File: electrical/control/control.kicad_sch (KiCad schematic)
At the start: 43 parts, among them J1 USB4105-GF-A, J2 SWD, J3 TC2030-NL, J4 UART, J5 QWIIC, SW1 SYS, U1 USBLC6-2P6, U2 LP5912-3.3DRV, U3 W25Q16JVSNIQ, U4 RP2040, U5 ABPMRRV060MG2A3, Y1 ABM8-272-T3

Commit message: More PCB work
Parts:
- U3: value W25Q16JVSNIQ -> W25Q16JVUXIQ; footprint Package_SO:SOIC-8_3.9x4.9mm_P1.27mm -> Package_SON:Winbond_USON-8-1EP_3x2mm_P0.5mm_EP0.2x1.6mm; LCSC C115407 -> C2843335
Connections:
- net I2C_SCL: now also U4.14 (GPIO11); no longer U4.38 (GPIO26_ADC0)
- net I2C_SDA: now also U4.13 (GPIO10); no longer U4.39 (GPIO27_ADC1)
- net PRESSURE_INT: now also U4.12 (GPIO9); no longer U4.40 (GPIO28_ADC2)
- net UART_RX: now also R5.2; no longer R5.1
- net UART_TX: now also R4.2; no longer R4.1
- net at SW1.1: now also U4.36 (GPIO24); no longer U4.5 (GPIO3)
- net at U4.3 (GPIO1): no longer R5.2
- net at U4.2 (GPIO0): no longer R4.2
- net at U4.27 (GPIO16): now also R4.1
- net at U4.28 (GPIO17): now also R5.1
- net at U4.37 (GPIO25): now also R8.1
- net at U4.4 (GPIO2): no longer R8.1
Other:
- moved on the sheet: D1, R4, R5, R8, SW1

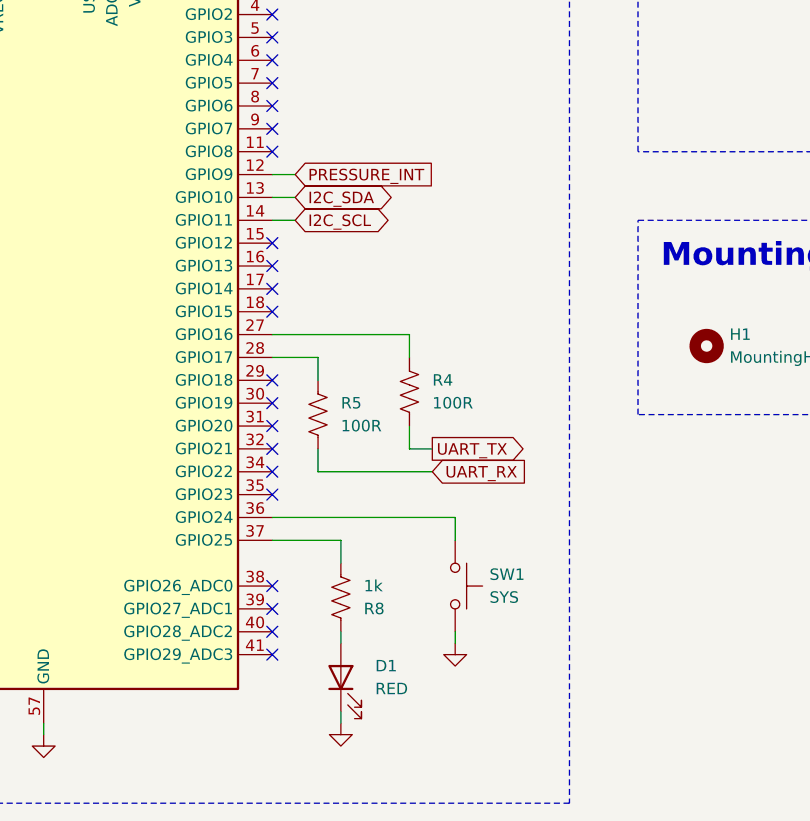
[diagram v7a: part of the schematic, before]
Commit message: All nets routed for control board
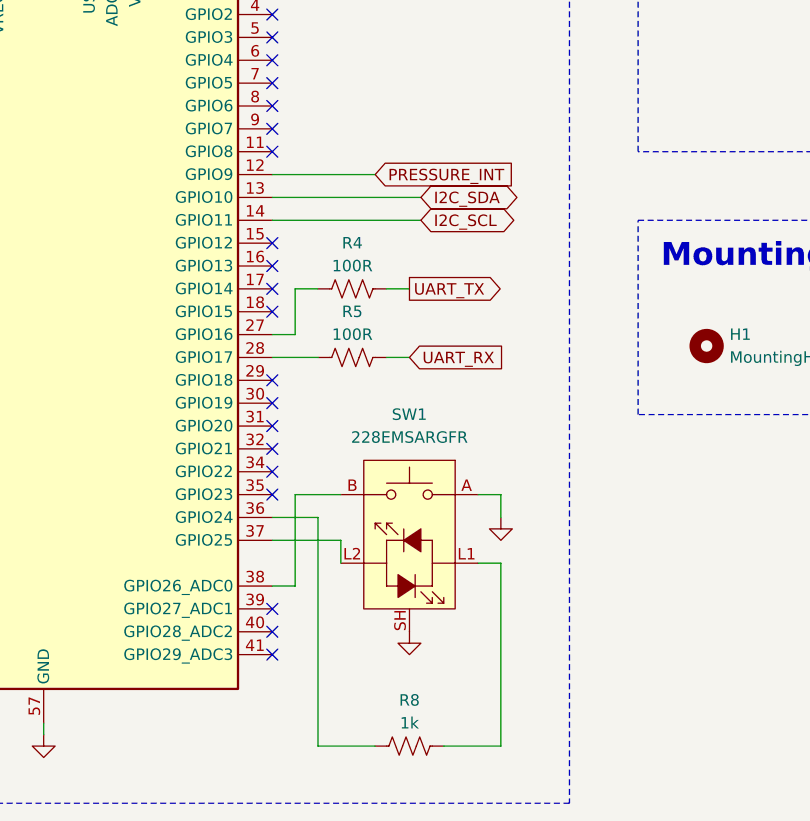
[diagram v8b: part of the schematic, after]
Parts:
- removed D1: RED, LED_SMD:LED_0603_1608Metric, symbol Device:LED
- removed SW1: SYS, Button_Switch_SMD:Panasonic_EVQPUL_EVQPUC, symbol Switch:SW_Push
- added SW1: 228EMSARGFR, midi_concertina:CTS_228EMS, symbol midi_concertina:CTS_228E
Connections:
- net GND: now also SW1.A, SW1.SH (Shield)
- net at R8.2: now also SW1.L1
- net at U4.36 (GPIO24): now also R8.1
- net at U4.37 (GPIO25): now also SW1.L2; no longer R8.1
- net at U4.38 (GPIO26_ADC0): now also SW1.B
- no-connect marks 28 -> 27
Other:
- moved on the sheet: R4, R5, R8
